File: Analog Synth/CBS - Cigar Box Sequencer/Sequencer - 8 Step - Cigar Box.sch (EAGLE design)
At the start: 204 parts, among them IC1 TL084P, IC10 79L05, IC11 MCP6002, IC12 74AC138N, IC13 74ALS04N, IC14 74AC138N, IC15 74ALS04N, IC16 74ALS04N, IC17 74ALS08N, IC2 TL084P, IC3 TL084P, IC4 74ALS04N, IC5 4050N, IC6 78L05, IC7 40193N, IC8 78L05, IC9 74LS86N, Q1 I/O, Q14 J310, Q15 J310, Q16 J310, Q17 J310, Q18 J310, Q19 J310, Q2 I/O, Q20 J310, Q3 I/O, Q4 2N3906, Q5 2N3904, Q6 J310, X1 I/O, X2 I/O, X3 I/O

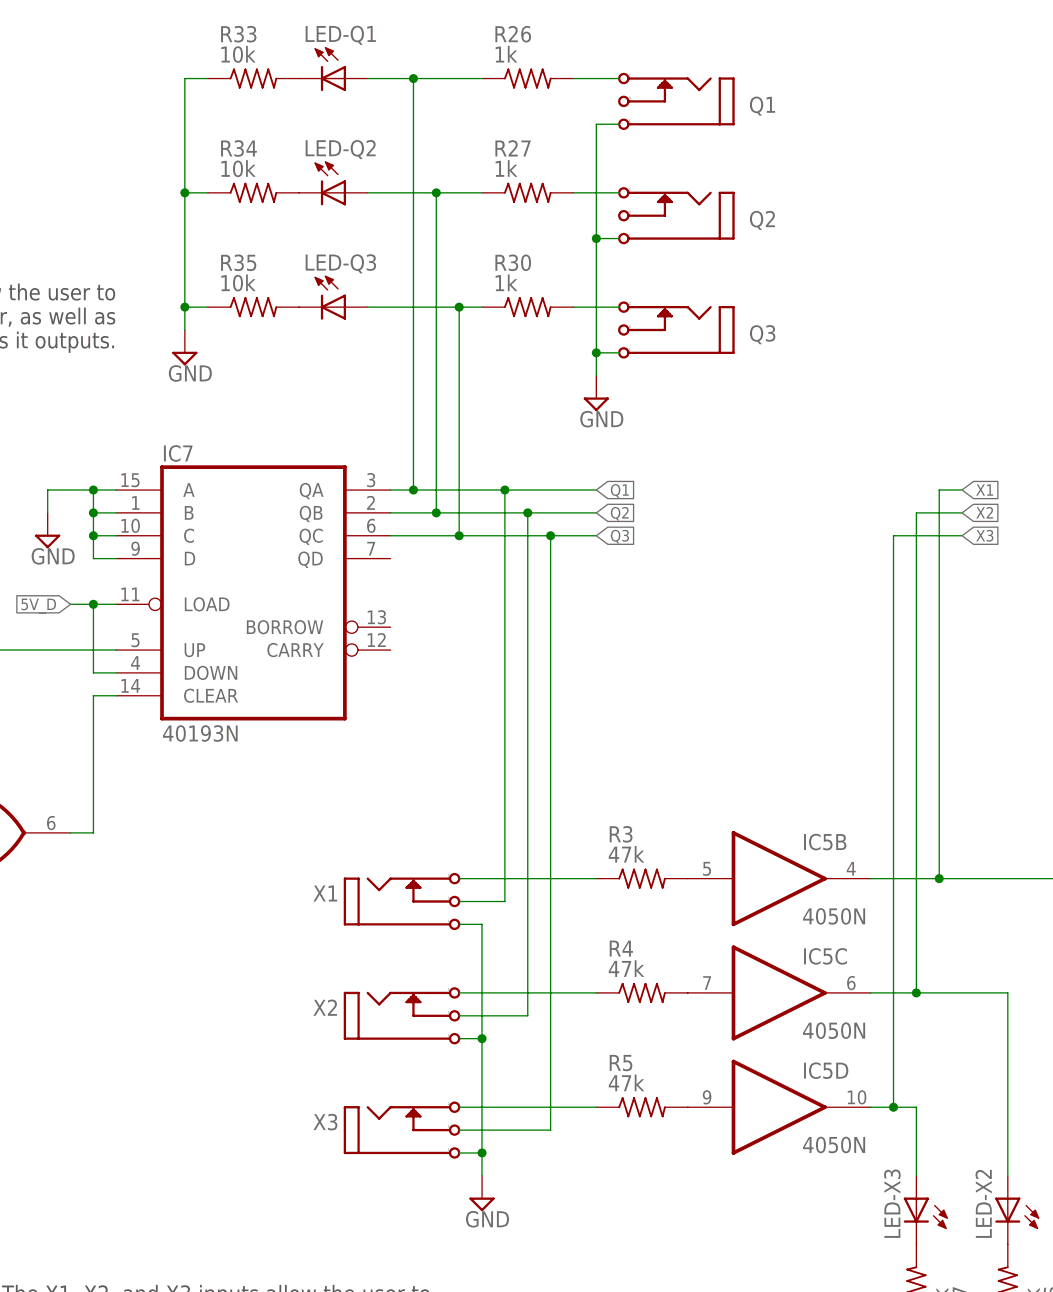
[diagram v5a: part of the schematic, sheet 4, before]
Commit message: CBS: changed the binary input/output bypass connections so that the user cannot short the outputs of the 193 binary counter.
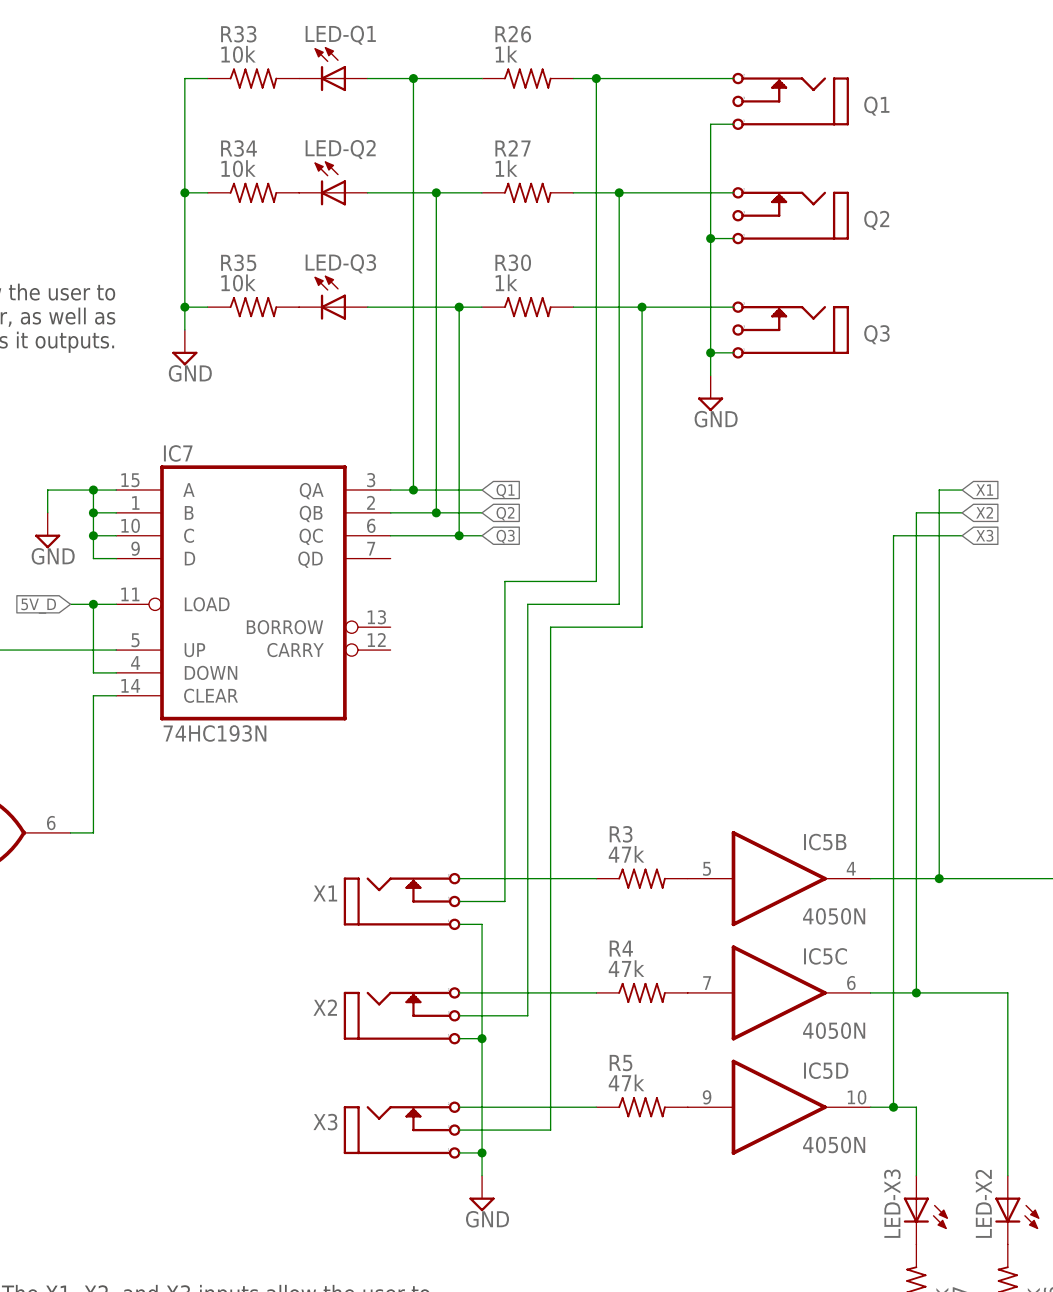
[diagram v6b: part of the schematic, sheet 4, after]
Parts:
- IC7: value 40193N -> 74HC193N
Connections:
- removed net N$11: Q1.P2, R26.2
- removed net N$23: Q2.P2, R27.2
- removed net N$24: Q3.P2, R30.2
- new net N$123: Q3.P2, R30.2, X3.P3
- new net N$52: Q1.P2, R26.2, X1.P3
- new net N$53: Q2.P2, R27.2, X2.P3
- net Q1: no longer X1.P3
- net Q2: no longer X2.P3
- net Q3: no longer X3.P3
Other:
- moved on the sheet: Q1, Q2, Q3
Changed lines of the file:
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@@
 <part name="R18" library="rcl" deviceset="R-US_" device="R0603" value="10k"/>
 <part name="SUPPLY4" library="supply2" deviceset="GND" device=""/>
-<part name="IC7" library="40xx" deviceset="40193" device="N"/>
+<part name="IC7" library="40xx" deviceset="40193" device="N" value="74HC193N"/>
 <part name="SUPPLY5" library="supply2" deviceset="GND" device=""/>
 <part name="SUPPLY16" library="supply2" deviceset="GND" device=""/>
@@
 <instance part="IC9" gate="D" x="-116.84" y="5.08" rot="MR180"/>
 <instance part="SUPPLY16" gate="GND" x="-76.2" y="15.24"/>
-<instance part="Q1" gate="J1" x="-5.08" y="63.5" smashed="yes" rot="MR0">
-<attribute name="NAME" x="4.826" y="62.23" size="1.778" layer="96" rot="MR0"/>
-</instance>
-<instance part="Q2" gate="J1" x="-5.08" y="50.8" smashed="yes" rot="MR0">
-<attribute name="NAME" x="4.826" y="49.53" size="1.778" layer="96" rot="MR0"/>
-</instance>
-<instance part="Q3" gate="J1" x="-5.08" y="38.1" smashed="yes" rot="MR0">
-<attribute name="NAME" x="4.826" y="36.83" size="1.778" layer="96" rot="MR0"/>
+<instance part="Q1" gate="J1" x="7.62" y="63.5" smashed="yes" rot="MR0">
+<attribute name="NAME" x="17.526" y="62.23" size="1.778" layer="96" rot="MR0"/>
+</instance>
+<instance part="Q2" gate="J1" x="7.62" y="50.8" smashed="yes" rot="MR0">
+<attribute name="NAME" x="17.526" y="49.53" size="1.778" layer="96" rot="MR0"/>
+</instance>
+<instance part="Q3" gate="J1" x="7.62" y="38.1" smashed="yes" rot="MR0">
+<attribute name="NAME" x="17.526" y="36.83" size="1.778" layer="96" rot="MR0"/>
 </instance>
 <instance part="R26" gate="G$1" x="-22.86" y="66.04" smashed="yes">
@@
 <attribute name="VALUE" x="-47.752" y="34.925" size="1.778" layer="96"/>
 </instance>
-<instance part="SUPPLY17" gate="GND" x="-15.24" y="30.48"/>
+<instance part="SUPPLY17" gate="GND" x="-2.54" y="30.48"/>
 <instance part="R33" gate="G$1" x="-53.34" y="66.04" smashed="yes">
 <attribute name="NAME" x="-57.15" y="70.0786" size="1.778" layer="95"/>
@@
 <segment>
 <pinref part="Q1" gate="J1" pin="P$1"/>
-<wire x1="-12.7" y1="60.96" x2="-15.24" y2="60.96" width="0.1524" layer="91"/>
+<wire x1="0" y1="60.96" x2="-2.54" y2="60.96" width="0.1524" layer="91"/>
 <pinref part="Q2" gate="J1" pin="P$1"/>
-<wire x1="-12.7" y1="48.26" x2="-15.24" y2="48.26" width="0.1524" layer="91"/>
-<wire x1="-15.24" y1="60.96" x2="-15.24" y2="48.26" width="0.1524" layer="91"/>
-<junction x="-15.24" y="48.26"/>
+<wire x1="0" y1="48.26" x2="-2.54" y2="48.26" width="0.1524" layer="91"/>
+<wire x1="-2.54" y1="60.96" x2="-2.54" y2="48.26" width="0.1524" layer="91"/>
+<junction x="-2.54" y="48.26"/>
 <pinref part="Q3" gate="J1" pin="P$1"/>
-<wire x1="-12.7" y1="35.56" x2="-15.24" y2="35.56" width="0.1524" layer="91"/>
-<wire x1="-15.24" y1="35.56" x2="-15.24" y2="33.02" width="0.1524" layer="91"/>
-<wire x1="-15.24" y1="48.26" x2="-15.24" y2="35.56" width="0.1524" layer="91"/>
-<junction x="-15.24" y="35.56"/>
+<wire x1="0" y1="35.56" x2="-2.54" y2="35.56" width="0.1524" layer="91"/>
+<wire x1="-2.54" y1="35.56" x2="-2.54" y2="33.02" width="0.1524" layer="91"/>
+<wire x1="-2.54" y1="48.26" x2="-2.54" y2="35.56" width="0.1524" layer="91"/>
+<junction x="-2.54" y="35.56"/>
 <pinref part="SUPPLY17" gate="GND" pin="GND"/>
 </segment>
@@
 <net name="Q1" class="0">
 <segment>
-<pinref part="X1" gate="J1" pin="P3"/>
-<wire x1="-30.48" y1="-25.4" x2="-25.4" y2="-25.4" width="0.1524" layer="91"/>
 <pinref part="IC7" gate="G$1" pin="QA"/>
 <wire x1="-38.1" y1="20.32" x2="-35.56" y2="20.32" width="0.1524" layer="91"/>
@@
 <wire x1="-35.56" y1="20.32" x2="-35.56" y2="66.04" width="0.1524" layer="91"/>
 <wire x1="-35.56" y1="66.04" x2="-27.94" y2="66.04" width="0.1524" layer="91"/>
-<wire x1="-35.56" y1="20.32" x2="-25.4" y2="20.32" width="0.1524" layer="91"/>
 <junction x="-35.56" y="20.32"/>
 <pinref part="LED-Q1" gate="G$1" pin="A"/>
 <wire x1="-40.64" y1="66.04" x2="-35.56" y2="66.04" width="0.1524" layer="91"/>
 <junction x="-35.56" y="66.04"/>
-<wire x1="-25.4" y1="-25.4" x2="-25.4" y2="20.32" width="0.1524" layer="91"/>
-<wire x1="-25.4" y1="20.32" x2="-15.24" y2="20.32" width="0.1524" layer="91"/>
-<junction x="-25.4" y="20.32"/>
-<label x="-15.24" y="20.32" size="1.27" layer="95" xref="yes"/>
+<wire x1="-35.56" y1="20.32" x2="-27.94" y2="20.32" width="0.1524" layer="91"/>
+<label x="-27.94" y="20.32" size="1.27" layer="95" xref="yes"/>
 </segment>
 </net>
 <net name="Q2" class="0">
 <segment>
-<pinref part="X2" gate="J1" pin="P3"/>
-<wire x1="-30.48" y1="-38.1" x2="-22.86" y2="-38.1" width="0.1524" layer="91"/>
 <pinref part="IC7" gate="G$1" pin="QB"/>
 <wire x1="-38.1" y1="17.78" x2="-33.02" y2="17.78" width="0.1524" layer="91"/>
@@
 <pinref part="R27" gate="G$1" pin="1"/>
 <junction x="-33.02" y="17.78"/>
-<wire x1="-33.02" y1="17.78" x2="-22.86" y2="17.78" width="0.1524" layer="91"/>
-<label x="-15.24" y="17.78" size="1.27" layer="95" xref="yes"/>
+<wire x1="-33.02" y1="17.78" x2="-27.94" y2="17.78" width="0.1524" layer="91"/>
+<label x="-27.94" y="17.78" size="1.27" layer="95" xref="yes"/>
 <pinref part="LED-Q2" gate="G$1" pin="A"/>
-<wire x1="-22.86" y1="17.78" x2="-15.24" y2="17.78" width="0.1524" layer="91"/>
 <wire x1="-40.64" y1="53.34" x2="-33.02" y2="53.34" width="0.1524" layer="91"/>
 <junction x="-33.02" y="53.34"/>
-<wire x1="-22.86" y1="-38.1" x2="-22.86" y2="17.78" width="0.1524" layer="91"/>
-<junction x="-22.86" y="17.78"/>
 </segment>
 </net>
 <net name="Q3" class="0">
 <segment>
-<pinref part="X3" gate="J1" pin="P3"/>
-<wire x1="-30.48" y1="-50.8" x2="-20.32" y2="-50.8" width="0.1524" layer="91"/>
 <pinref part="IC7" gate="G$1" pin="QC"/>
 <wire x1="-38.1" y1="15.24" x2="-30.48" y2="15.24" width="0.1524" layer="91"/>
@@
 <pinref part="R30" gate="G$1" pin="1"/>
 <junction x="-30.48" y="15.24"/>
-<wire x1="-30.48" y1="15.24" x2="-20.32" y2="15.24" width="0.1524" layer="91"/>
-<label x="-15.24" y="15.24" size="1.27" layer="95" xref="yes"/>
+<wire x1="-30.48" y1="15.24" x2="-27.94" y2="15.24" width="0.1524" layer="91"/>
+<label x="-27.94" y="15.24" size="1.27" layer="95" xref="yes"/>
 <pinref part="LED-Q3" gate="G$1" pin="A"/>
-<wire x1="-20.32" y1="15.24" x2="-15.24" y2="15.24" width="0.1524" layer="91"/>
 <wire x1="-40.64" y1="40.64" x2="-30.48" y2="40.64" width="0.1524" layer="91"/>
 <junction x="-30.48" y="40.64"/>
-<wire x1="-20.32" y1="-50.8" x2="-20.32" y2="15.24" width="0.1524" layer="91"/>
-<junction x="-20.32" y="15.24"/>
-</segment>
-</net>
-<net name="N$11" class="0">
-<segment>
-<pinref part="R26" gate="G$1" pin="2"/>
-<pinref part="Q1" gate="J1" pin="P2"/>
-<wire x1="-12.7" y1="66.04" x2="-17.78" y2="66.04" width="0.1524" layer="91"/>
-</segment>
-</net>
-<net name="N$23" class="0">
-<segment>
-<pinref part="R27" gate="G$1" pin="2"/>
-<pinref part="Q2" gate="J1" pin="P2"/>
-<wire x1="-12.7" y1="53.34" x2="-17.78" y2="53.34" width="0.1524" layer="91"/>
-</segment>
-</net>
-<net name="N$24" class="0">
-<segment>
-<pinref part="R30" gate="G$1" pin="2"/>
-<pinref part="Q3" gate="J1" pin="P2"/>
-<wire x1="-12.7" y1="40.64" x2="-17.78" y2="40.64" width="0.1524" layer="91"/>
 </segment>
 </net>
@@
 </segment>
 </net>
+<net name="N$52" class="0">
+<segment>
+<pinref part="X1" gate="J1" pin="P3"/>
+<wire x1="-30.48" y1="-25.4" x2="-25.4" y2="-25.4" width="0.1524" layer="91"/>
+<wire x1="-25.4" y1="-25.4" x2="-25.4" y2="10.16" width="0.1524" layer="91"/>
+<wire x1="-25.4" y1="10.16" x2="-15.24" y2="10.16" width="0.1524" layer="91"/>
+<pinref part="R26" gate="G$1" pin="2"/>
+<pinref part="Q1" gate="J1" pin="P2"/>
+<wire x1="0" y1="66.04" x2="-15.24" y2="66.04" width="0.1524" layer="91"/>
+<wire x1="-15.24" y1="66.04" x2="-17.78" y2="66.04" width="0.1524" layer="91"/>
+<wire x1="-15.24" y1="10.16" x2="-15.24" y2="66.04" width="0.1524" layer="91"/>
+<junction x="-15.24" y="66.04"/>
+</segment>
+</net>
+<net name="N$53" class="0">
+<segment>
+<pinref part="X2" gate="J1" pin="P3"/>
+<wire x1="-30.48" y1="-38.1" x2="-22.86" y2="-38.1" width="0.1524" layer="91"/>
+<wire x1="-22.86" y1="-38.1" x2="-22.86" y2="7.62" width="0.1524" layer="91"/>
+<pinref part="R27" gate="G$1" pin="2"/>
+<pinref part="Q2" gate="J1" pin="P2"/>
+<wire x1="0" y1="53.34" x2="-12.7" y2="53.34" width="0.1524" layer="91"/>
+<wire x1="-12.7" y1="53.34" x2="-17.78" y2="53.34" width="0.1524" layer="91"/>
+<wire x1="-22.86" y1="7.62" x2="-12.7" y2="7.62" width="0.1524" layer="91"/>
+<wire x1="-12.7" y1="7.62" x2="-12.7" y2="53.34" width="0.1524" layer="91"/>
+<junction x="-12.7" y="53.34"/>
+</segment>
+</net>
+<net name="N$123" class="0">
+<segment>
+<pinref part="X3" gate="J1" pin="P3"/>
+<wire x1="-30.48" y1="-50.8" x2="-20.32" y2="-50.8" width="0.1524" layer="91"/>
+<wire x1="-20.32" y1="-50.8" x2="-20.32" y2="5.08" width="0.1524" layer="91"/>
+<pinref part="R30" gate="G$1" pin="2"/>
+<pinref part="Q3" gate="J1" pin="P2"/>
+<wire x1="0" y1="40.64" x2="-10.16" y2="40.64" width="0.1524" layer="91"/>
+<wire x1="-10.16" y1="40.64" x2="-17.78" y2="40.64" width="0.1524" layer="91"/>
+<wire x1="-20.32" y1="5.08" x2="-10.16" y2="5.08" width="0.1524" layer="91"/>
+<wire x1="-10.16" y1="5.08" x2="-10.16" y2="40.64" width="0.1524" layer="91"/>
+<junction x="-10.16" y="40.64"/>
+</segment>
+</net>

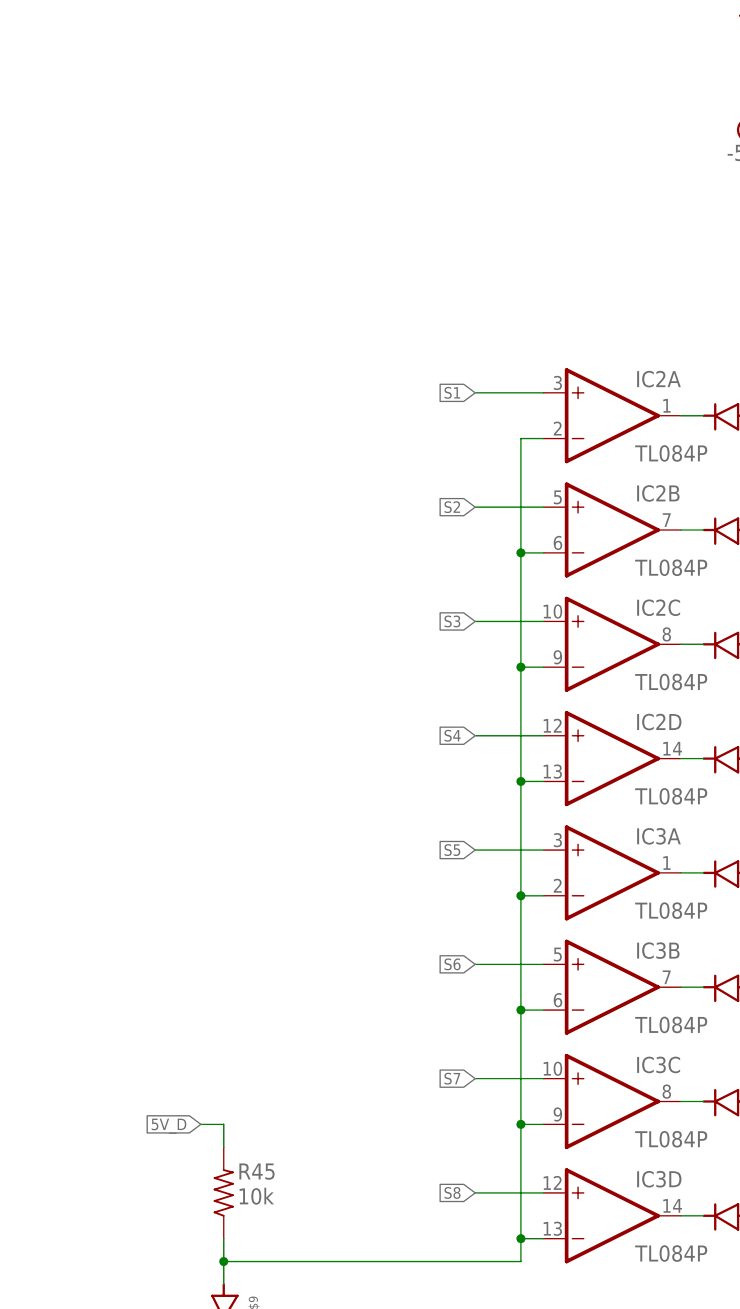
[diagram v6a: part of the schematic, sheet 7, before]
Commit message: CBS: updating schematic and generating another pdf.
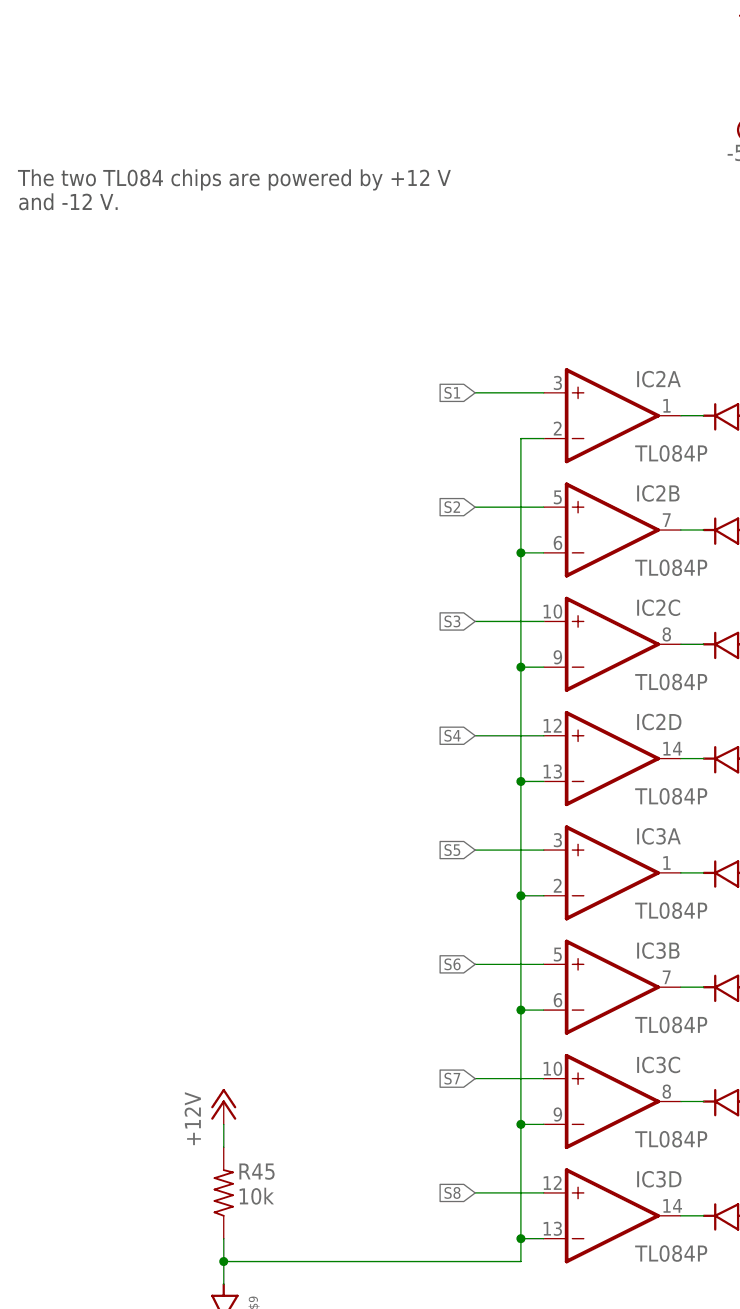
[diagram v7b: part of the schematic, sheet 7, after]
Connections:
- removed net N$12: LED2.DP
- net +12V: now also R45.2
- net 5V_D: no longer R45.2
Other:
- note added: "The two TL084 chips are powered by +12 V and -12 V."
- note added: "This 2-pole 6-throw switch selects the number of steps in the sequence and displays it on the seven-segment LED display"
- note removed: "This switch selects the number of steps in the sequence and displays it on the seven- segment LED display"
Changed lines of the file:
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@@
 <part name="R69" library="rcl" deviceset="R-US_" device="R0603" value="1k"/>
 <part name="SUPPLY51" library="supply2" deviceset="GND" device=""/>
+<part name="P+6" library="supply1" deviceset="+12V" device=""/>
 </parts>
 <sheets>
@@
 <wire x1="87.122" y1="33.782" x2="87.122" y2="34.036" width="0.1524" layer="95"/>
 <text x="66.04" y="73.66" size="1.778" layer="97">Number of Steps Indicator</text>
-<text x="58.42" y="-12.7" size="1.778" layer="97">This switch selects the number of steps in the
-sequence and displays it on the seven-
-segment LED display</text>
+<text x="58.42" y="-12.7" size="1.778" layer="97">This 2-pole 6-throw switch selects the number
+of steps in the sequence and displays it on
+the seven-segment LED display</text>
 </plain>
 <instances>
@@
 <wire x1="81.28" y1="30.48" x2="82.55" y2="31.75" width="0.1524" layer="91"/>
 <wire x1="81.28" y1="30.48" x2="80.01" y2="29.21" width="0.1524" layer="91"/>
-</segment>
-</net>
-<net name="N$12" class="0">
-<segment>
-<pinref part="LED2" gate="G$1" pin="DP"/>
-<wire x1="109.22" y1="48.26" x2="111.76" y2="48.26" width="0.1524" layer="91"/>
-<label x="111.76" y="48.26" size="2.54" layer="95" xref="yes"/>
 </segment>
 </net>
@@
 be activated at a time because they are
 controlled by the demultiplexer.</text>
+<text x="-43.18" y="81.28" size="1.778" layer="97">The two TL084 chips are powered by +12 V
+and -12 V.</text>
 </plain>
 <instances>
@@
 </instance>
 <instance part="SUPPLY36" gate="GND" x="-20.32" y="-45.72"/>
+<instance part="P+6" gate="1" x="-20.32" y="-17.78"/>
 </instances>
 <busses>
@@
 </segment>
 </net>
-<net name="5V_D" class="0">
+<net name="GND" class="0">
+<segment>
+<pinref part="SUPPLY36" gate="GND" pin="GND"/>
+<pinref part="U$9" gate="D1" pin="CATHODE"/>
+</segment>
+</net>
+<net name="+12V" class="0">
 <segment>
 <pinref part="R45" gate="G$1" pin="2"/>
 <wire x1="-20.32" y1="-22.86" x2="-20.32" y2="-20.32" width="0.1524" layer="91"/>
-<wire x1="-20.32" y1="-20.32" x2="-22.86" y2="-20.32" width="0.1524" layer="91"/>
-<label x="-22.86" y="-20.32" size="1.27" layer="95" rot="R180" xref="yes"/>
-</segment>
-</net>
-<net name="GND" class="0">
-<segment>
-<pinref part="SUPPLY36" gate="GND" pin="GND"/>
-<pinref part="U$9" gate="D1" pin="CATHODE"/>
-</segment>
-</net>
+<pinref part="P+6" gate="1" pin="+12V"/>
+</segment>
+</net>
